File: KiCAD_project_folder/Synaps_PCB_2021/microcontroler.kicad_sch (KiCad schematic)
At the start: 9 parts

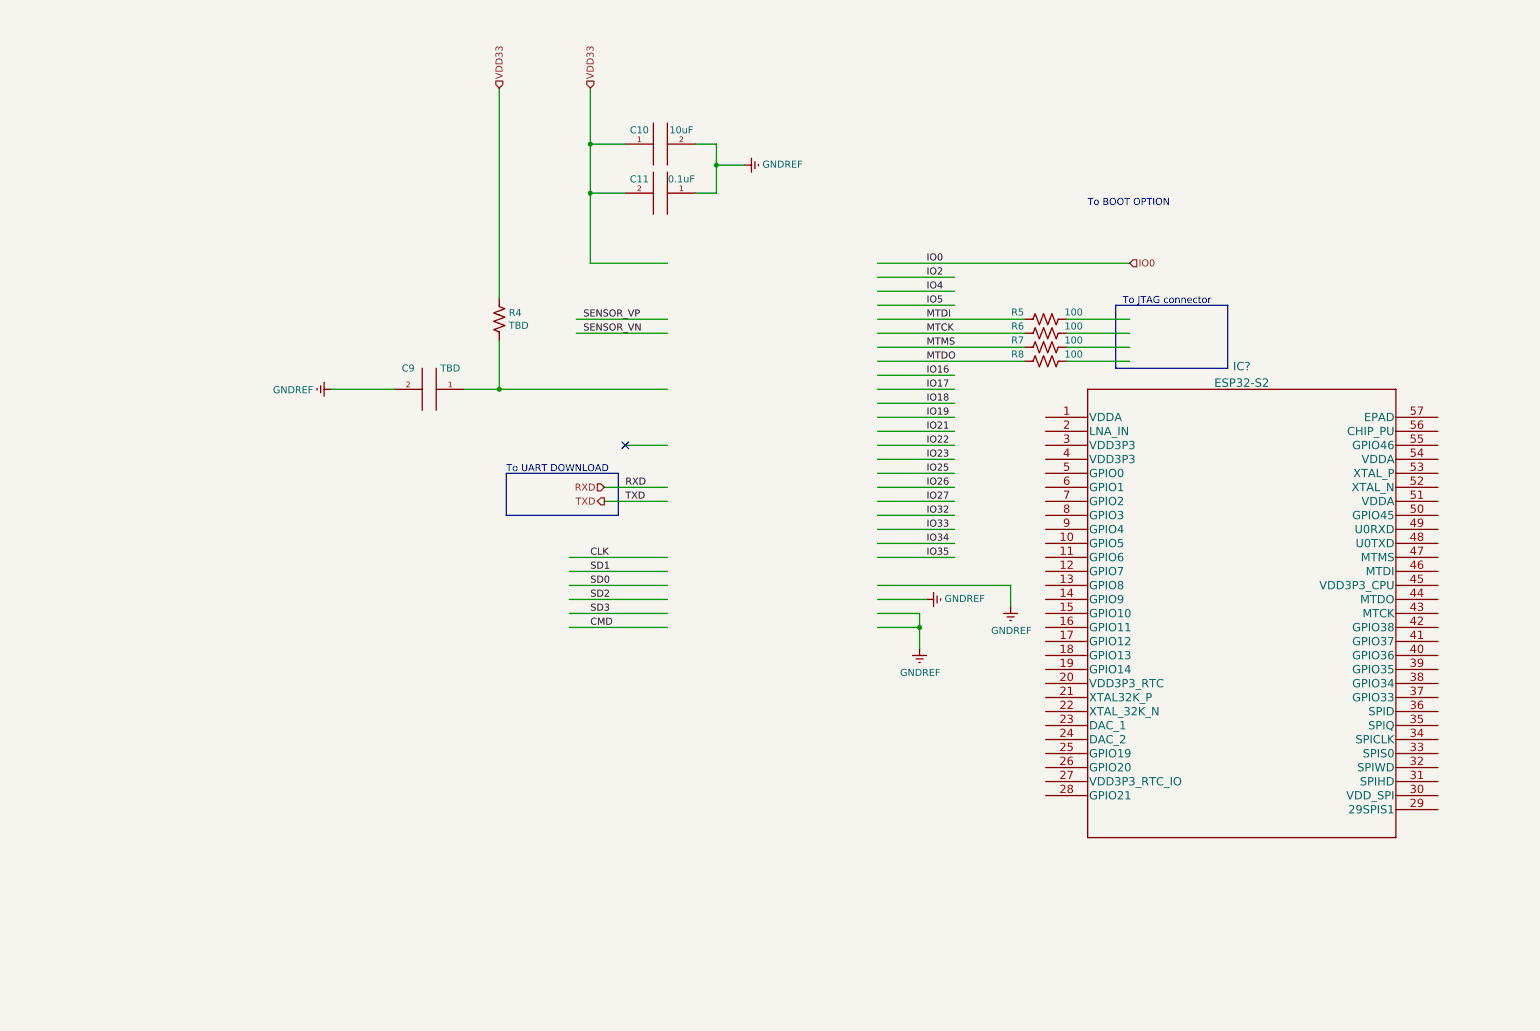
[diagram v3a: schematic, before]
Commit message: Added Esp32-S2 datasheet files and hardware design guidelines to project
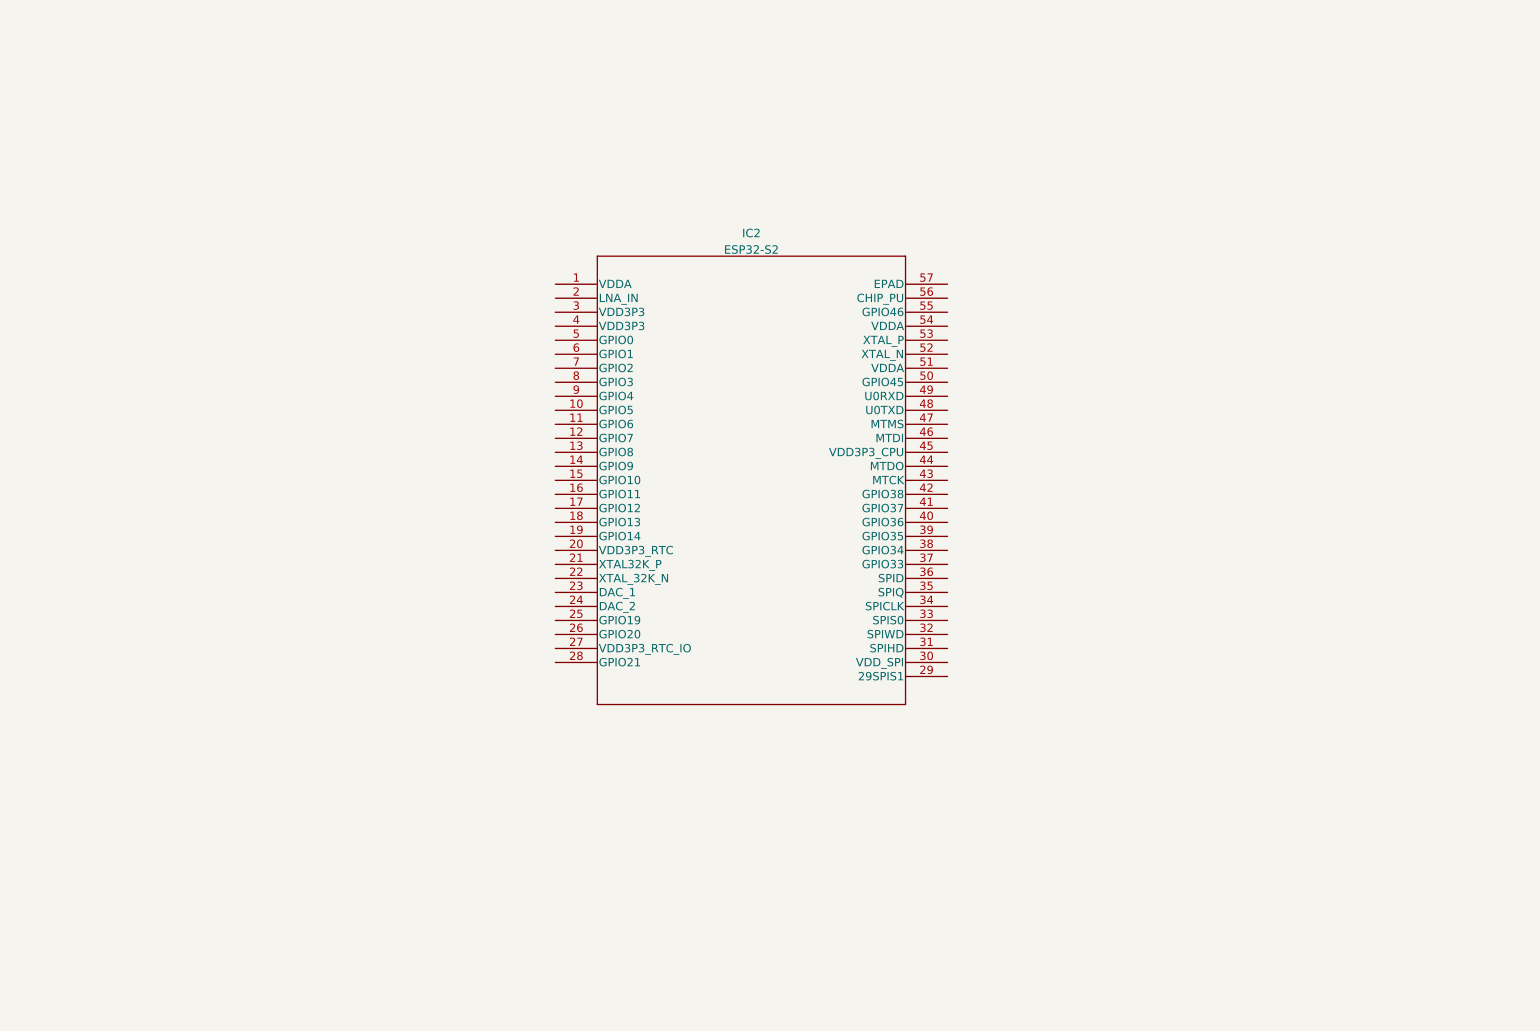
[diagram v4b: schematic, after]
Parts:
- removed C10: 10uF, Capacitor_SMD:C_1206_3216Metric_Pad1.33x1.80mm_HandSolder, symbol pspice:CAP
- removed C11: 0.1uF, Capacitor_SMD:C_1206_3216Metric_Pad1.33x1.80mm_HandSolder, symbol pspice:CAP
- removed C9: TBD, Capacitor_SMD:C_1206_3216Metric_Pad1.33x1.80mm_HandSolder, symbol pspice:CAP
- removed R4: TBD, Resistor_SMD:R_1206_3216Metric_Pad1.30x1.75mm_HandSolder, symbol Device:R_US
- removed R5, R6, R7, R8: 100, Resistor_SMD:R_1206_3216Metric_Pad1.30x1.75mm_HandSolder, symbol Device:R_US
- gave numbers to parts that had none: 1
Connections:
- no-connect marks 1 -> 0
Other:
- note removed: "To BOOT OPTION"
- note removed: "To JTAG connector"
- note removed: "To UART DOWNLOAD"
- moved on the sheet: IC2

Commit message: Microcontrolling routing and pin assigment
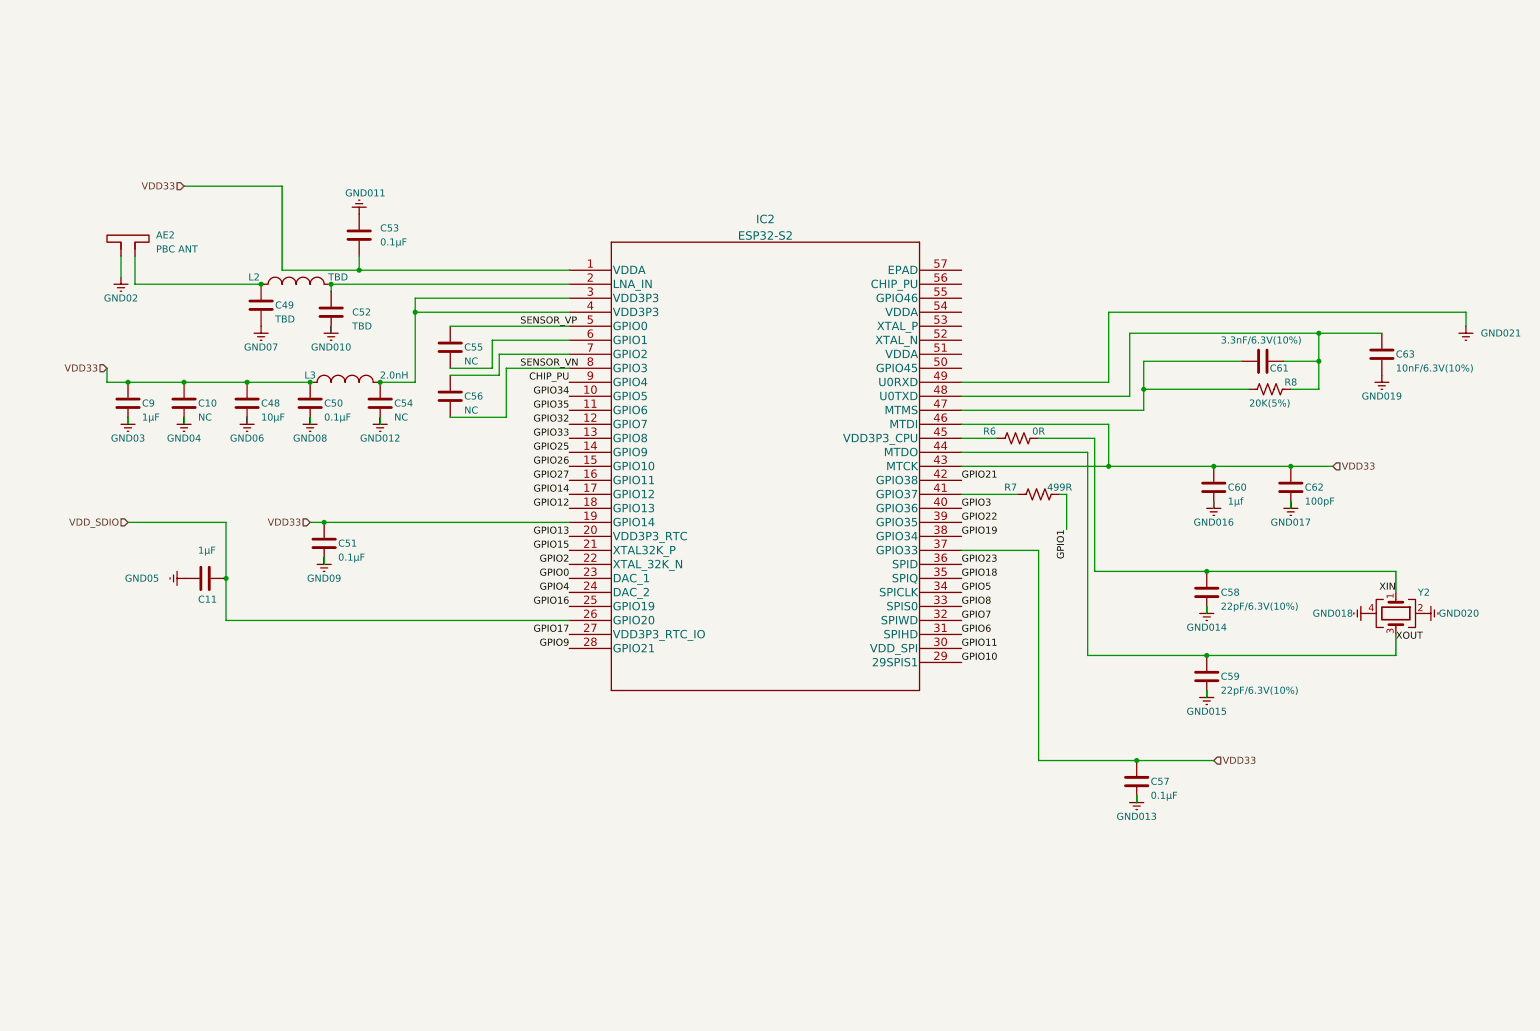
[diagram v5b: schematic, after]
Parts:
- added AE2: PBC ANT, symbol Device:Antenna_Dipole
- added C10, C54, C55, C56: NC, symbol Device:C
- added C11, C9: 1µF, symbol Device:C
- added C48: 10µF, symbol Device:C
- added C49, C52: TBD, symbol Device:C
- added C50, C51, C53, C57: 0.1µF, symbol Device:C
- added C58, C59: 22pF/6.3V(10%), symbol Device:C
- added C60: 1µf, symbol Device:C
- added C61: 3.3nF/6.3V(10%), symbol Device:C
- added C62: 100pF, symbol Device:C
- added C63: 10nF/6.3V(10%), symbol Device:C
- added L2: TBD, symbol pspice:INDUCTOR
- added L3: 2.0nH, symbol pspice:INDUCTOR
- added R6: 0R, symbol Device:R_US
- added R7: 499R, symbol Device:R_US
- added R8: 20K(5%), symbol Device:R_US
- added Y2: Crystal_GND24, symbol Device:Crystal_GND24
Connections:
- net VDD33: now reaches IC2.1 (VDDA)
- net VDD33: now also IC2.19 (GPIO14), IC2.37 (GPIO33), IC2.43 (MTCK), IC2.46 (MTDI), C10.1, C48.1, C50.1, C51.1, C53.2, C57.1, C60.1, C62.1, C9.1, L3.1
- net GPIO34: now reaches IC2.10 (GPIO5)
- net GPIO35: now reaches IC2.11 (GPIO6)
- net GPIO32: now reaches IC2.12 (GPIO7)
- net GPIO33: now reaches IC2.13 (GPIO8)
- net GPIO25: now reaches IC2.14 (GPIO9)
- net GPIO26: now reaches IC2.15 (GPIO10)
- net GPIO27: now reaches IC2.16 (GPIO11)
- net GPIO14: now reaches IC2.17 (GPIO12)
- net GPIO12: now reaches IC2.18 (GPIO13)
- net at IC2.2 (LNA_IN): now also C52.1, L2.2
- net GPIO13: now reaches IC2.20 (VDD3P3_RTC)
- net GPIO15: now reaches IC2.21 (XTAL32K_P)
- net GPIO2: now reaches IC2.22 (XTAL_32K_N)
- net GPIO0: now reaches IC2.23 (DAC_1)
- net GPIO4: now reaches IC2.24 (DAC_2)
- net GPIO16: now reaches IC2.25 (GPIO19)
- net VDD_SDIO: now reaches IC2.26 (GPIO20)
- net VDD_SDIO: now also C11.1
- net GPIO17: now reaches IC2.27 (VDD3P3_RTC_IO)
- net GPIO9: now reaches IC2.28 (GPIO21)
- net GPIO10: now reaches IC2.29 (29SPIS1)
- net at IC2.3 (VDD3P3): now also IC2.4 (VDD3P3), C54.1, L3.2
- net GPIO11: now reaches IC2.30 (VDD_SPI)
- net GPIO6: now reaches IC2.31 (SPIHD)
- net GPIO7: now reaches IC2.32 (SPIWD)
- net GPIO8: now reaches IC2.33 (SPIS0)
- net GPIO5: now reaches IC2.34 (SPICLK)
- net GPIO18: now reaches IC2.35 (SPIQ)
- net GPIO23: now reaches IC2.36 (SPID)
- net GPIO19: now reaches IC2.38 (GPIO34)
- net GPIO22: now reaches IC2.39 (GPIO35)
- net GPIO3: now reaches IC2.40 (GPIO36)
- net at IC2.41 (GPIO37): now also R7.2
- net GPIO21: now reaches IC2.42 (GPIO38)
- net XOUT: now reaches IC2.44 (MTDO)
- net XOUT: now also C59.1, Y2.3
- net at IC2.45 (VDD3P3_CPU): now also R6.2
- net at IC2.47 (MTMS): now also C61.2, R8.2
- net at IC2.48 (U0TXD): now also C61.1, C63.1, R8.1
- net Earth: now reaches IC2.49 (U0RXD)
- net Earth: now also AE2.1, C10.2, C11.2, C48.2, C49.2, C50.2, C51.2, C52.2, C53.1, C54.2, C57.2, C58.2, C59.2, C60.2, C62.2, C63.2, C9.2, Y2.2, Y2.4
- net SENSOR_VP: now reaches IC2.5 (GPIO0)
- net SENSOR_VP: now also C55.1
- net at IC2.6 (GPIO1): now also C55.2
- net at IC2.7 (GPIO2): now also C56.1
- net SENSOR_VN: now reaches IC2.8 (GPIO3)
- net SENSOR_VN: now also C56.2
- net CHIP_PU: now reaches IC2.9 (GPIO4)
- new net: AE2.2, C49.1, L2.1
- new net GPIO1: R7.1
- new net XIN: C58.1, R6.1, Y2.1

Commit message: Added footprints to powersupply schematic and started placing components on PCB
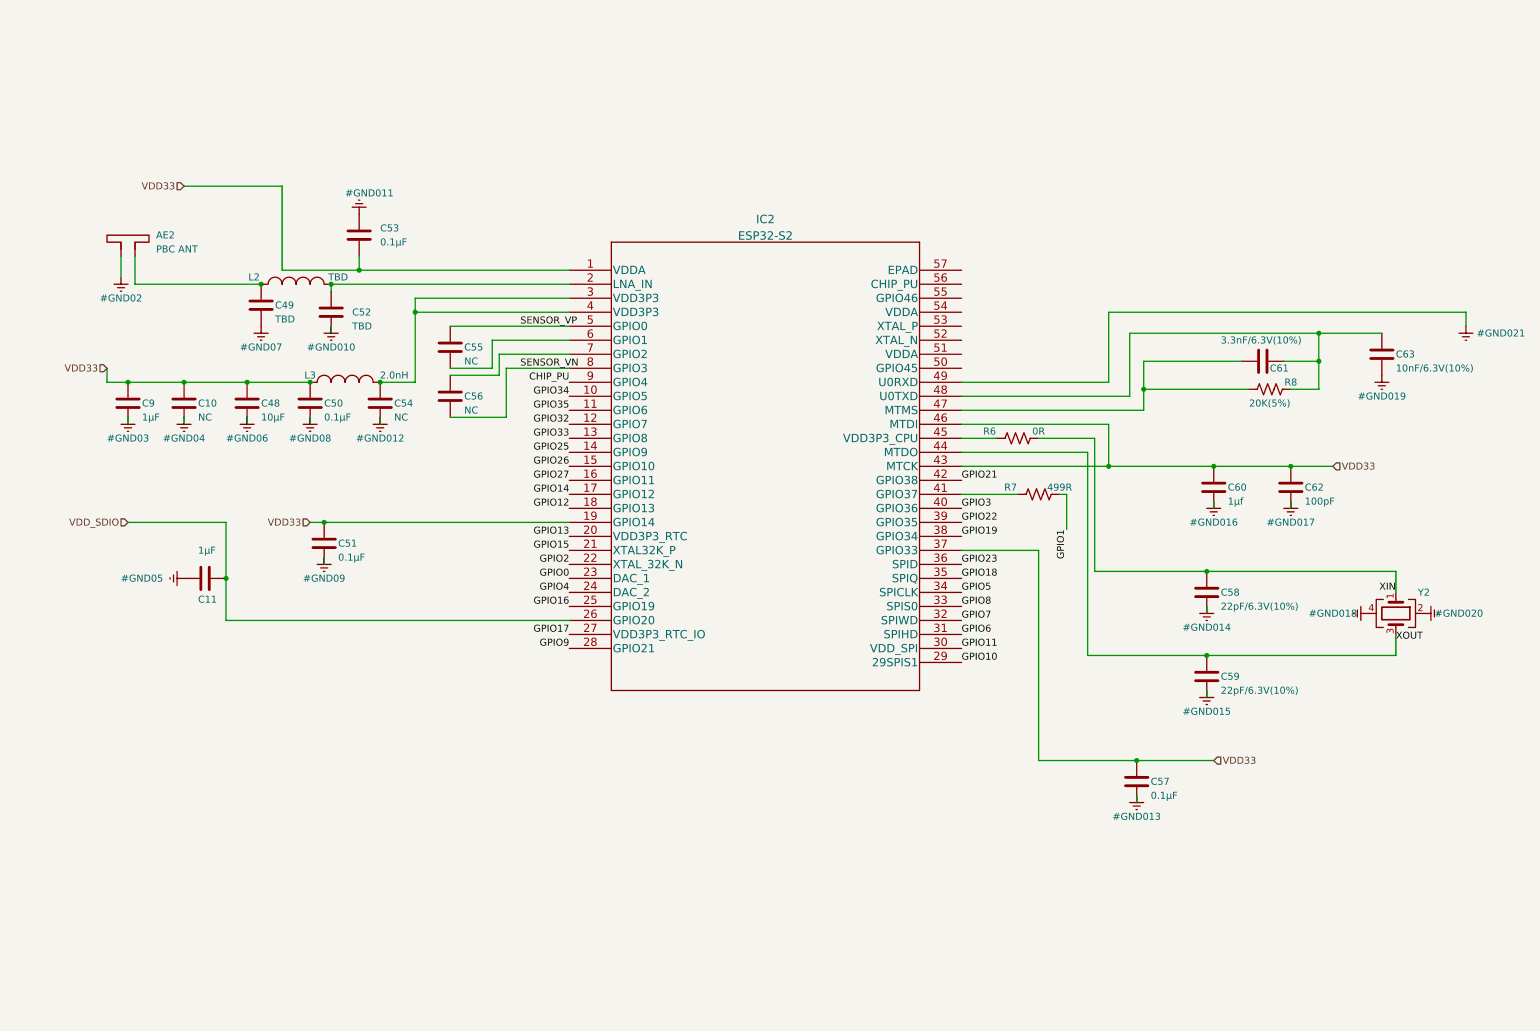
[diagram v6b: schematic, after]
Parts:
- AE2: footprint (none) -> RF_Antenna:Texas_SWRA117D_2.4GHz_Left
- C10, C11, C48, C49, C50, C51, C52, C53, C54, C55, C56, C57, C58, C59, C60, C61, C62, C63, C9: footprint (none) -> Capacitor_SMD:C_1206_3216Metric_Pad1.33x1.80mm_HandSolder
- IC2: footprint QFN56_ESP32_7X7_EXP -> ESP32-S2:ESP32-S2
- L2, L3: footprint (none) -> Inductor_SMD:L_1206_3216Metric_Pad1.22x1.90mm_HandSolder
- R6, R7, R8: footprint (none) -> Resistor_SMD:R_1206_3216Metric_Pad1.30x1.75mm_HandSolder
